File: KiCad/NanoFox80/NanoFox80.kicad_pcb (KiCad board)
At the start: 2 copper layers, 90 x 37 mm, 82 parts, among them J101 Conn_01x02, J103 Conn_01x01, J104 Conn_01x02, J105 Conn_01x02, J106 Conn_01x02, J107 Conn_01x02, J108 Conn_01x01, J109 Conn_01x02, J110 I2C, J111 DB9 Female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

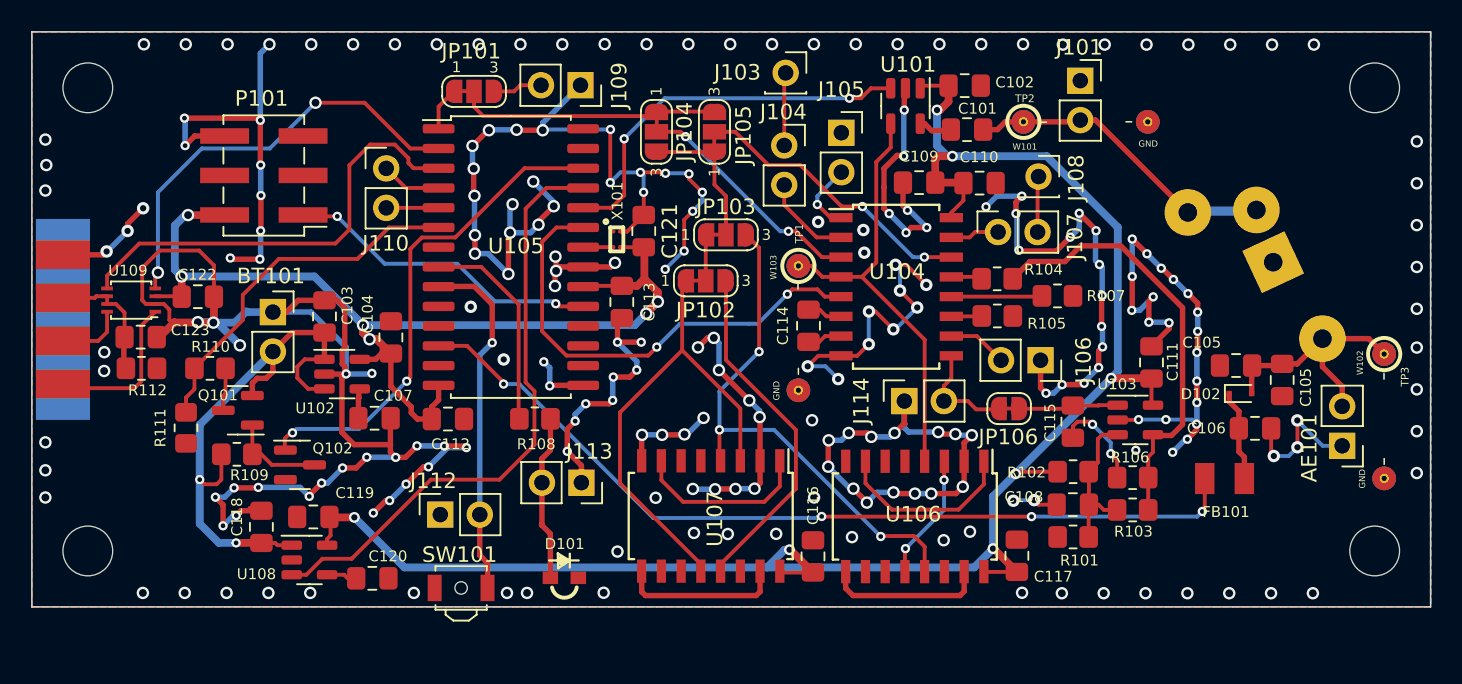
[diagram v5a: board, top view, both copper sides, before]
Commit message: PCB Updates
o Added holes for scope probe ground clips
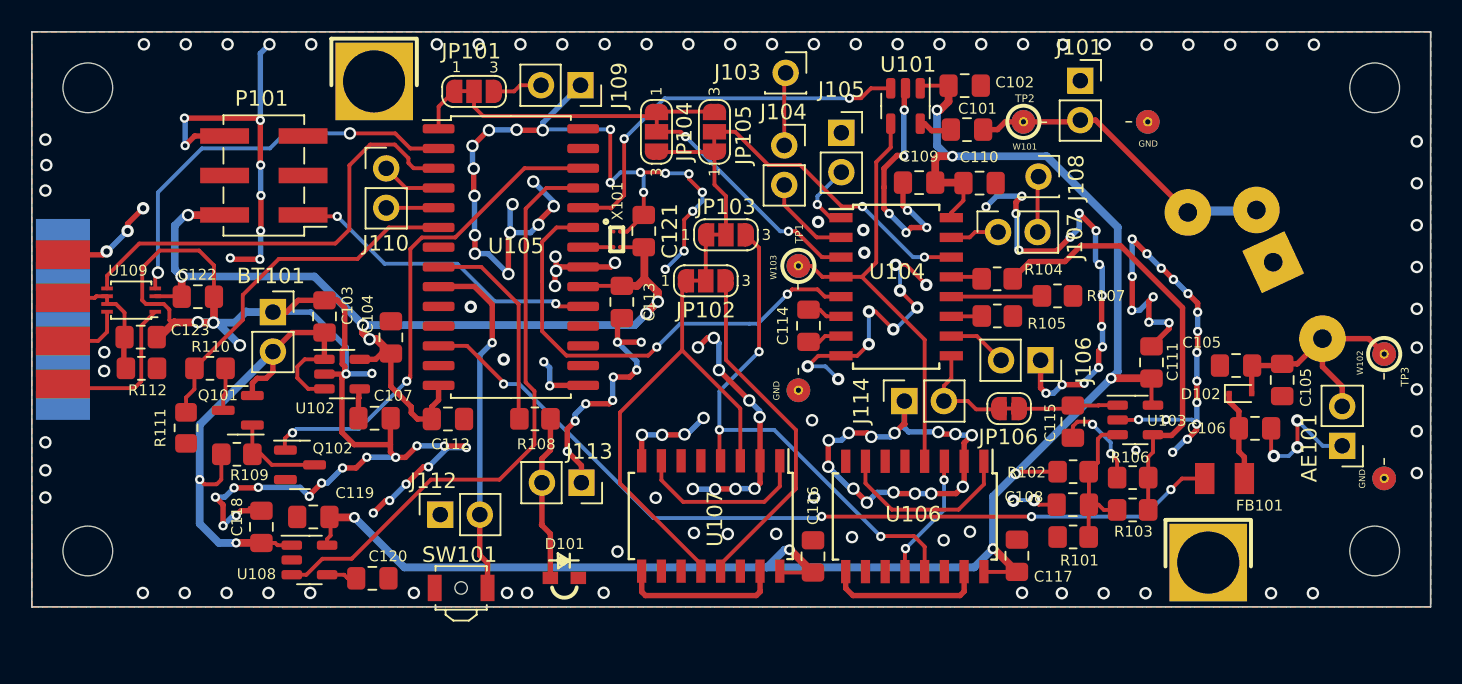
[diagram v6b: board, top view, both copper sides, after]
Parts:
- added W308: CONN_01X01, Pin_Headers:Pin_Header_Straight_1x01, F.Cu at (102.0, 59.2)
- added W308: CONN_01X01, Pin_Headers:Pin_Header_Straight_1x01, F.Cu at (155.7, 90.1)
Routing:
- net Net-(U105-Pad2): track 27.9 -> 26.3 mm
- net Net-(U105-Pad12): track 56.2 -> 55.0 mm
- net GND: vias 232 -> 228
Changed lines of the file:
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@@
       ))
   )
+  (footprint "Pin_Headers:Pin_Header_Straight_1x01" (layer "F.Cu")
+    (at 102.02 59.1875)
+    (descr "Through hole pin header")
+    (tags "pin header")
+    (attr through_hole)
+    (fp_text reference "W308" (at 0 -3.35) (layer "F.SilkS") hide
+      (effects (font (size 0.4 0.4) (thickness 0.1)))
+    )
+    (fp_text value "CONN_01X01" (at 0 -3.1) (layer "F.Fab")
+      (effects (font (size 1 1) (thickness 0.15)))
+    )
+    (fp_line (start -2.75 0.25) (end -2.75 -2.75) (layer "F.SilkS") (width 0.25))
+    (fp_line (start -2.75 -2.75) (end 2.7 -2.75) (layer "F.SilkS") (width 0.25))
+    (fp_line (start 2.75 -2.75) (end 2.75 0.25) (layer "F.SilkS") (width 0.25))
+    (pad "1" thru_hole rect locked (at 0 0) (size 5 5) (drill 4) (layers *.Cu *.Mask "F.SilkS")
+      (zone_connect 1) (thermal_width 0.75) (thermal_gap 0.4))
+    (model "Pin_Headers.3dshapes/Pin_Header_Straight_1x01.wrl"
+      (offset (xyz 0 0 0))
+      (scale (xyz 1 1 1))
+      (rotate (xyz 0 0 90))
+    )
+  )
   (footprint "Connector_PinSocket_2.54mm:PinSocket_1x02_P2.54mm_Vertical" (layer "F.Cu")
     (at 95.51 74.03)
@@
     (property "Sheetname" "")
     (attr smd)
-    (fp_text reference "FB101" (at -0.09 -2.15 unlocked) (layer "F.SilkS")
+    (fp_text reference "FB101" (at -2.25 -1.74 unlocked) (layer "F.SilkS")
       (effects (font (size 0.7 0.7) (thickness 0.15)))
     )
@@
     )
   )
+  (footprint "Pin_Headers:Pin_Header_Straight_1x01" (layer "F.Cu")
+    (at 155.69 90.1475)
+    (descr "Through hole pin header")
+    (tags "pin header")
+    (attr through_hole)
+    (fp_text reference "W308" (at 4.87 -1.2975) (layer "F.SilkS") hide
+      (effects (font (size 0.4 0.4) (thickness 0.1)))
+    )
+    (fp_text value "CONN_01X01" (at 0 -3.1) (layer "F.Fab")
+      (effects (font (size 1 1) (thickness 0.15)))
+    )
+    (fp_line (start 2.75 -2.75) (end 2.75 0.25) (layer "F.SilkS") (width 0.25))
+    (fp_line (start -2.75 0.25) (end -2.75 -2.75) (layer "F.SilkS") (width 0.25))
+    (fp_line (start -2.75 -2.75) (end 2.7 -2.75) (layer "F.SilkS") (width 0.25))
+    (pad "1" thru_hole rect locked (at 0 0) (size 5 5) (drill 4) (layers *.Cu *.Mask "F.SilkS")
+      (zone_connect 1) (thermal_width 0.75) (thermal_gap 0.4))
+    (model "Pin_Headers.3dshapes/Pin_Header_Straight_1x01.wrl"
+      (offset (xyz 0 0 0))
+      (scale (xyz 1 1 1))
+      (rotate (xyz 0 0 90))
+    )
+  )
   (footprint "Package_TO_SOT_SMD:SOT-23" (layer "F.Cu")
     (at 93.25 80.35 180)
@@
     (clearance 0.2)
     (attr smd)
-    (fp_text reference "U103" (at -1.1775 -2.3) (layer "F.SilkS")
+    (fp_text reference "U103" (at 2.0225 0.05) (layer "F.SilkS")
       (effects (font (size 0.7 0.7) (thickness 0.15)))
     )
@@
   (via (at 122.242 56.79) (size 0.8) (drill 0.5) (layers "F.Cu" "B.Cu") (free) (net 1))
   (via (at 93.01 85.34) (size 0.6) (drill 0.3) (layers "F.Cu" "B.Cu") (net 1))
-  (via (at 154.348 92.12) (size 0.8) (drill 0.5) (layers "F.Cu" "B.Cu") (free) (net 1))
   (via (at 135.43 75.14) (size 0.8) (drill 0.4) (layers "F.Cu" "B.Cu") (net 1))
   (via (at 159.798 56.82) (size 0.8) (drill 0.5) (layers "F.Cu" "B.Cu") (free) (net 1))
@@
   (via (at 119.16 65.04) (size 0.6) (drill 0.3) (layers "F.Cu" "B.Cu") (net 1))
   (via (at 93.386725 76.168719) (size 0.8) (drill 0.5) (layers "F.Cu" "B.Cu") (net 1))
-  (via (at 157.04 92.12) (size 0.8) (drill 0.5) (layers "F.Cu" "B.Cu") (free) (net 1))
   (via (at 110.57 92.1) (size 0.8) (drill 0.5) (layers "F.Cu" "B.Cu") (free) (net 1))
   (via (at 148.474225 68.79553) (size 0.6) (drill 0.3) (layers "F.Cu" "B.Cu") (net 1))
@@
   (via (at 143.32 67.69) (size 0.6) (drill 0.3) (layers "F.Cu" "B.Cu") (net 1))
   (via (at 101.55 83.37) (size 0.6) (drill 0.3) (layers "F.Cu" "B.Cu") (net 1))
-  (via (at 100.67 56.8) (size 0.8) (drill 0.5) (layers "F.Cu" "B.Cu") (free) (net 1))
   (via (at 136.133371 61.030019) (size 0.6) (drill 0.3) (layers "F.Cu" "B.Cu") (net 1))
   (via (at 123.22 80.84) (size 0.8) (drill 0.5) (layers "F.Cu" "B.Cu") (net 1))
@@
   (via (at 151.21 80.95) (size 0.6) (drill 0.3) (layers "F.Cu" "B.Cu") (net 1))
   (via (at 146.29 78.7) (size 0.6) (drill 0.3) (layers "F.Cu" "B.Cu") (net 1))
-  (via (at 103.362 56.8) (size 0.8) (drill 0.5) (layers "F.Cu" "B.Cu") (free) (net 1))
   (via (at 84.65 77.82) (size 0.8) (drill 0.5) (layers "F.Cu" "B.Cu") (free) (net 1))
   (via (at 152.97 80.95) (size 0.6) (drill 0.3) (layers "F.Cu" "B.Cu") (net 1))
@@
   (segment (start 163.04 75.74) (end 166.02 75.74) (width 0.35) (layer "F.Cu") (net 83))
   (segment (start 161.4175 77.3625) (end 163.04 75.74) (width 0.35) (layer "F.Cu") (net 83))
+  (segment (start 154 84.74) (end 155.465 84.74) (width 0.25) (layer "F.Cu") (net 84))
   (segment (start 108.005 76.205) (end 108.72 76.92) (width 0.25) (layer "F.Cu") (net 84))
   (segment (start 110.35 78.55) (end 110.35 78.66) (width 0.25) (layer "F.Cu") (net 84))
+  (segment (start 153.29 85.45) (end 154 84.74) (width 0.25) (layer "F.Cu") (net 84))
   (segment (start 108.72 76.92) (end 110.35 78.55) (width 0.25) (layer "F.Cu") (net 84))
   (segment (start 106.17 76.205) (end 108.005 76.205) (width 0.25) (layer "F.Cu") (net 84))
   (segment (start 130.83 87.19) (end 144.32 87.19) (width 0.25) (layer "F.Cu") (net 84))
-  (segment (start 155.31 86.76) (end 155.465 86.605) (width 0.25) (layer "F.Cu") (net 84))
-  (segment (start 155.465 86.605) (end 155.465 84.74) (width 0.25) (layer "F.Cu") (net 84))
   (segment (start 130.82 87.18) (end 130.83 87.19) (width 0.25) (layer "F.Cu") (net 84))
-  (segment (start 155.31 86.86) (end 155.31 86.76) (width 0.25) (layer "F.Cu") (net 84))
   (via (at 144.32 87.19) (size 0.6) (drill 0.3) (layers "F.Cu" "B.Cu") (net 84))
-  (via (at 155.31 86.86) (size 0.6) (drill 0.3) (layers "F.Cu" "B.Cu") (net 84))
+  (via (at 153.29 85.45) (size 0.6) (drill 0.3) (layers "F.Cu" "B.Cu") (net 84))
   (via (at 130.82 87.18) (size 0.6) (drill 0.3) (layers "F.Cu" "B.Cu") (net 84))
   (via (at 110.35 78.66) (size 0.6) (drill 0.3) (layers "F.Cu" "B.Cu") (net 84))
   (segment (start 119.984022 87.28) (end 111.364022 78.66) (width 0.25) (layer "B.Cu") (net 84))
   (segment (start 130.82 87.18) (end 130.72 87.28) (width 0.25) (layer "B.Cu") (net 84))
-  (segment (start 154.98 87.19) (end 155.31 86.86) (width 0.25) (layer "B.Cu") (net 84))
-  (segment (start 144.32 87.19) (end 154.98 87.19) (width 0.25) (layer "B.Cu") (net 84))
+  (segment (start 153.29 85.45) (end 151.55 87.19) (width 0.25) (layer "B.Cu") (net 84))
+  (segment (start 151.55 87.19) (end 144.32 87.19) (width 0.25) (layer "B.Cu") (net 84))
   (segment (start 111.364022 78.66) (end 110.35 78.66) (width 0.25) (layer "B.Cu") (net 84))
   (segment (start 130.72 87.28) (end 119.984022 87.28) (width 0.25) (layer "B.Cu") (net 84))
@@
   (segment (start 87.94 74.01) (end 87.04 74.91) (width 0.25) (layer "F.Cu") (net 86))
   (segment (start 82.26952 78.92452) (end 82 78.655) (width 0.25) (layer "F.Cu") (net 86))
+  (segment (start 104.355 63.505) (end 106.17 63.505) (width 0.25) (layer "F.Cu") (net 87))
   (segment (start 87.94 72.51) (end 87.94 71.66) (width 0.25) (layer "F.Cu") (net 87))
-  (segment (start 101.41 60.56) (end 104.355 63.505) (width 0.25) (layer "F.Cu") (net 87))
   (segment (start 87.94 71.66) (end 88.11 71.49) (width 0.25) (layer "F.Cu") (net 87))
-  (segment (start 98.25 60.56) (end 101.41 60.56) (width 0.25) (layer "F.Cu") (net 87))
-  (segment (start 104.355 63.505) (end 106.17 63.505) (width 0.25) (layer "F.Cu") (net 87))
+  (segment (start 103.383838 62.533838) (end 104.355 63.505) (width 0.25) (layer "F.Cu") (net 87))
+  (segment (start 100.464757 62.533838) (end 103.383838 62.533838) (width 0.25) (layer "F.Cu") (net 87))
   (via (at 88.11 71.49) (size 0.8) (drill 0.5) (layers "F.Cu" "B.Cu") (net 87))
-  (via (at 98.25 60.56) (size 0.8) (drill 0.5) (layers "F.Cu" "B.Cu") (net 87))
+  (via (at 100.464757 62.533838) (size 0.8) (drill 0.5) (layers "F.Cu" "B.Cu") (net 87))
   (segment (start 95.31 63.5) (end 90.94 63.5) (width 0.25) (layer "B.Cu") (net 87))
   (segment (start 90.94 63.5) (end 88.11 66.33) (width 0.25) (layer "B.Cu") (net 87))
+  (segment (start 100.464757 62.533838) (end 96.276162 62.533838) (width 0.25) (layer "B.Cu") (net 87))
+  (segment (start 96.276162 62.533838) (end 95.31 63.5) (width 0.25) (layer "B.Cu") (net 87))
   (segment (start 88.11 66.33) (end 88.11 71.49) (width 0.25) (layer "B.Cu") (net 87))
-  (segment (start 98.25 60.56) (end 95.31 63.5) (width 0.25) (layer "B.Cu") (net 87))
   (segment (start 104.23 64.44) (end 104.565 64.775) (width 0.25) (layer "F.Cu") (net 88))
   (segment (start 101.77 63.25) (end 103.35 63.25) (width 0.25) (layer "F.Cu") (net 88))
